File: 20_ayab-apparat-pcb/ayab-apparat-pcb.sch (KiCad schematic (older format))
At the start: 8 parts, among them P10 CONN_2, U1 NCP1117ST50T3G

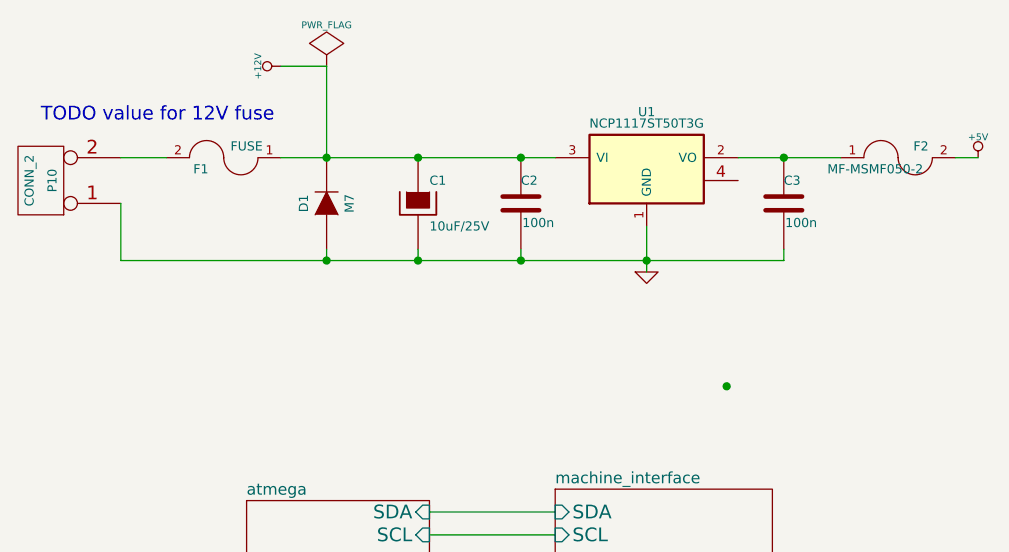
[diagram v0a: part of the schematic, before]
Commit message: BOM nearly done TODO add relais for autoswitch when USB 5V is connected to schematic
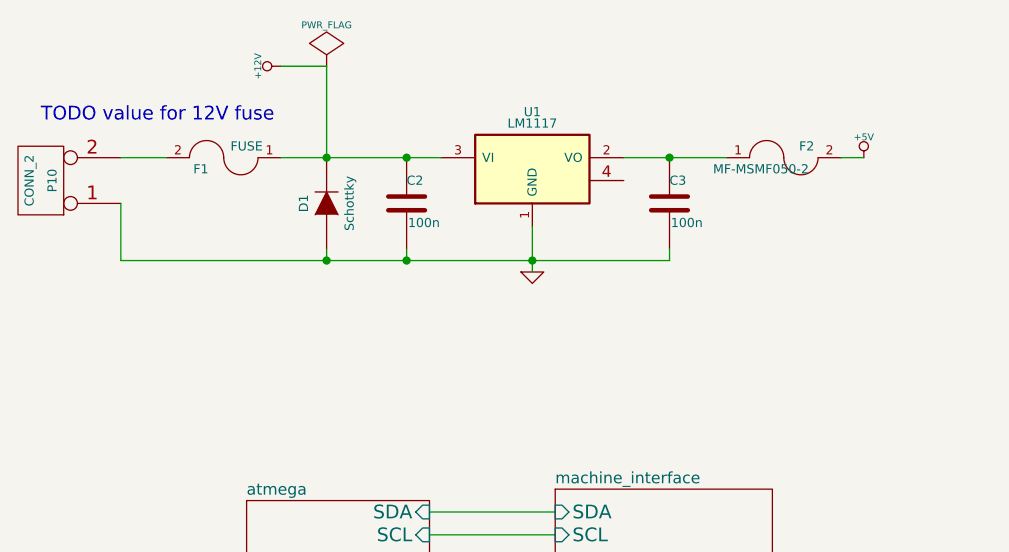
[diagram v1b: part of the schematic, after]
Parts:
- removed C1: 10uF/25V, symbol CAPAPOL
- D1: value M7 -> Schottky
- U1: value NCP1117ST50T3G -> LM1117
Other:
- moved on the sheet: C2, C3, F2, U1
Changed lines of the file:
@@
 $EndSheet
-$Comp
-L CAPAPOL C1
-U 1 1 52EAB7DE
-P 5400 2500
-F 0 "C1" H 5450 2600 40  0000 L CNN
-F 1 "10uF/25V" H 5450 2400 40  0000 L CNN
-F 2 "" H 5500 2350 30  0000 C CNN
-F 3 "" H 5400 2500 300 0000 C CNN
-	1    5400 2500
-	1    0    0    -1
-$EndComp
 $Comp
 L DIODE D1
@@
 P 5000 2500
 F 0 "D1" H 5000 2600 40  0000 C CNN
-F 1 "M7" H 5000 2400 40  0000 C CNN
+F 1 "Schottky" H 5000 2400 40  0000 C CNN
 F 2 "" H 5000 2500 60  0000 C CNN
 F 3 "" H 5000 2500 60  0000 C CNN
@@
 $EndComp
 $Comp
-L GND #PWR02
+L GND #PWR01
 U 1 1 52EABC97
-P 6400 2800
-F 0 "#PWR02" H 6400 2800 30  0001 C CNN
-F 1 "GND" H 6400 2730 30  0001 C CNN
-F 2 "" H 6400 2800 60  0000 C CNN
-F 3 "" H 6400 2800 60  0000 C CNN
-	1    6400 2800
+P 5900 2800
+F 0 "#PWR01" H 5900 2800 30  0001 C CNN
+F 1 "GND" H 5900 2730 30  0001 C CNN
+F 2 "" H 5900 2800 60  0000 C CNN
+F 3 "" H 5900 2800 60  0000 C CNN
+	1    5900 2800
 	1    0    0    -1
 $EndComp
@@
 L C C3
 U 1 1 52EAC19E
-P 7000 2500
-F 0 "C3" H 7000 2600 40  0000 L CNN
-F 1 "100n" H 7006 2415 40  0000 L CNN
-F 2 "" H 7038 2350 30  0000 C CNN
-F 3 "" H 7000 2500 60  0000 C CNN
-	1    7000 2500
+P 6500 2500
+F 0 "C3" H 6500 2600 40  0000 L CNN
+F 1 "100n" H 6506 2415 40  0000 L CNN
+F 2 "" H 6538 2350 30  0000 C CNN
+F 3 "" H 6500 2500 60  0000 C CNN
+	1    6500 2500
 	1    0    0    -1
 $EndComp
 $Comp
-L +5V #PWR03
+L +5V #PWR02
 U 1 1 52EAC279
-P 7850 2300
-F 0 "#PWR03" H 7850 2390 20  0001 C CNN
-F 1 "+5V" H 7850 2390 30  0000 C CNN
-F 2 "" H 7850 2300 60  0000 C CNN
-F 3 "" H 7850 2300 60  0000 C CNN
-	1    7850 2300
+P 7350 2300
+F 0 "#PWR02" H 7350 2390 20  0001 C CNN
+F 1 "+5V" H 7350 2390 30  0000 C CNN
+F 2 "" H 7350 2300 60  0000 C CNN
+F 3 "" H 7350 2300 60  0000 C CNN
+	1    7350 2300
 	1    0    0    -1
 $EndComp
 $Comp
-L +12V #PWR04
+L +12V #PWR03
 U 1 1 52EAEFAF
 P 4800 1900
-F 0 "#PWR04" H 4800 1850 20  0001 C CNN
+F 0 "#PWR03" H 4800 1850 20  0001 C CNN
 F 1 "+12V" H 4800 2000 30  0000 C CNN
 F 2 "" H 4800 1900 60  0000 C CNN
@@
 L FUSE F2
 U 1 1 52EAEFC3
-P 7500 2300
-F 0 "F2" H 7600 2350 40  0000 C CNN
-F 1 "MF-MSMF050-2" H 7400 2250 40  0000 C CNN
-F 2 "" H 7500 2300 60  0000 C CNN
-F 3 "" H 7500 2300 60  0000 C CNN
-	1    7500 2300
+P 7000 2300
+F 0 "F2" H 7100 2350 40  0000 C CNN
+F 1 "MF-MSMF050-2" H 6900 2250 40  0000 C CNN
+F 2 "" H 7000 2300 60  0000 C CNN
+F 3 "" H 7000 2300 60  0000 C CNN
+	1    7000 2300
 	1    0    0    -1
 $EndComp
@@
 TODO value for 12V fuse
 $Comp
-L PWR_FLAG #FLG05
+L PWR_FLAG #FLG04
 U 1 1 52EECA32
 P 5000 1900
-F 0 "#FLG05" H 5000 1995 30  0001 C CNN
+F 0 "#FLG04" H 5000 1995 30  0001 C CNN
 F 1 "PWR_FLAG" H 5000 2080 30  0000 C CNN
 F 2 "" H 5000 1900 60  0000 C CNN
@@
 L C C2
 U 1 1 52F1A256
-P 5850 2500
-F 0 "C2" H 5850 2600 40  0000 L CNN
-F 1 "100n" H 5856 2415 40  0000 L CNN
-F 2 "" H 5888 2350 30  0000 C CNN
-F 3 "" H 5850 2500 60  0000 C CNN
-	1    5850 2500
+P 5350 2500
+F 0 "C2" H 5350 2600 40  0000 L CNN
+F 1 "100n" H 5356 2415 40  0000 L CNN
+F 2 "" H 5388 2350 30  0000 C CNN
+F 3 "" H 5350 2500 60  0000 C CNN
+	1    5350 2500
 	1    0    0    -1
 $EndComp
@@
 L NCP1117ST50T3G U1
 U 1 1 52F1A2B7
-P 6400 2350
-F 0 "U1" H 6400 2600 40  0000 C CNN
-F 1 "NCP1117ST50T3G" H 6400 2550 40  0000 C CNN
-F 2 "" H 6400 2350 60  0000 C CNN
-F 3 "" H 6400 2350 60  0000 C CNN
-	1    6400 2350
+P 5900 2350
+F 0 "U1" H 5900 2600 40  0000 C CNN
+F 1 "LM1117" H 5900 2550 40  0000 C CNN
+F 2 "" H 5900 2350 60  0000 C CNN
+F 3 "" H 5900 2350 60  0000 C CNN
+	1    5900 2350
 	1    0    0    -1
 $EndComp
@@
 	5450 4700 6000 4700
 Wire Wire Line
-	4800 2300 6000 2300
+	4800 2300 5500 2300
 Wire Wire Line
-	6800 2300 7250 2300
+	6300 2300 6750 2300
 Wire Wire Line
-	4100 2750 7000 2750
-Connection ~ 7000 2300
+	4100 2750 6500 2750
+Connection ~ 6500 2300
 Wire Wire Line
-	7000 2750 7000 2700
+	6500 2750 6500 2700
 Wire Wire Line
-	7750 2300 7850 2300
+	7250 2300 7350 2300
 Wire Wire Line
 	5000 1900 5000 2300
@@
 Wire Wire Line
 	5000 2700 5000 2750
-Connection ~ 5400 2300
 Wire Wire Line
-	5400 2700 5400 2750
-Connection ~ 5400 2750
+	5350 2700 5350 2750
+Connection ~ 5350 2750
 Wire Wire Line
-	5850 2700 5850 2750
-Connection ~ 5850 2750
-Wire Wire Line
-	6400 2600 6400 2800
-Connection ~ 6400 2750
-Connection ~ 5850 2300
-Connection ~ 6750 3300
+	5900 2600 5900 2800
+Connection ~ 5900 2750
+Connection ~ 5350 2300
 Wire Wire Line
 	4100 2300 4300 2300

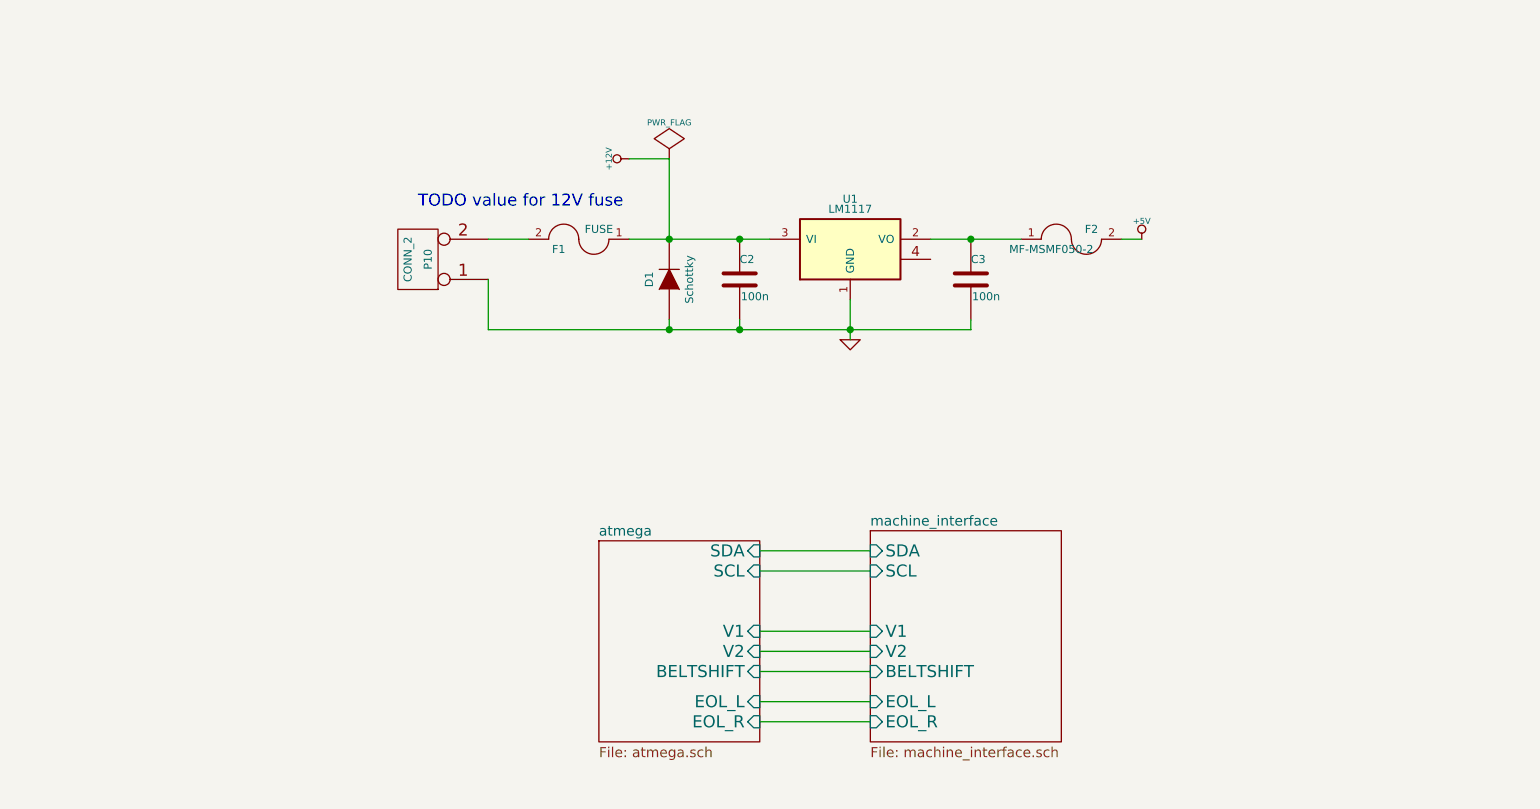
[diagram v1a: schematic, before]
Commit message: Added automatic switching between ATmega and original machine control when VUSB is attached
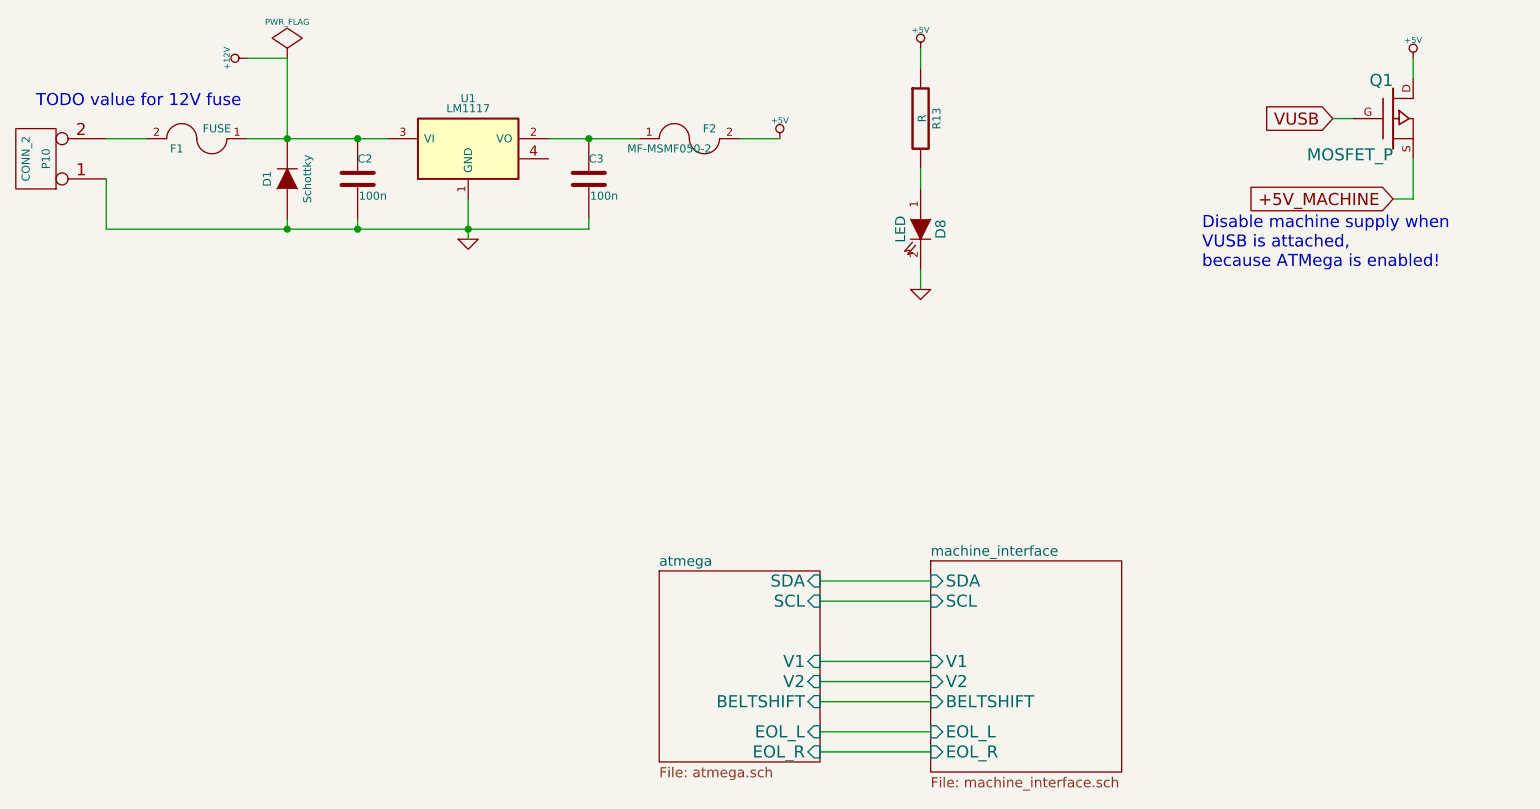
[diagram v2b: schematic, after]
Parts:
- added D8: LED, symbol LED
- added Q1: MOSFET_P, symbol MOSFET_P
- added R13: R, symbol R
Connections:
- net +5V: now also Q1.D, R13.1
- net GND: now also D8.2 (K)
- new net: D8.1 (A), R13.2
- new net +5V_MACHINE: Q1.S
- new net VUSB: Q1.G
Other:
- note added: "Disable machine supply when\nVUSB is attached,\nbecause ATMega is enabled!"
- moved on the sheet: C2, C3, D1, F1, F2, P10, U1

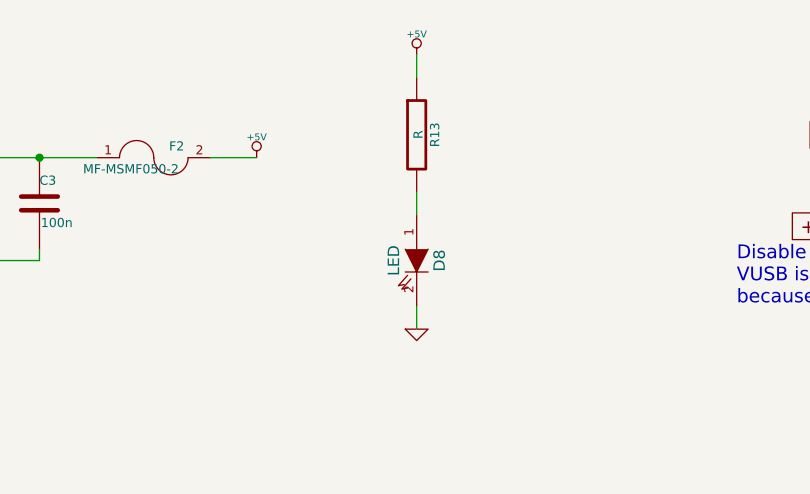
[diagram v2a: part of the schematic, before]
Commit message: Changed power supply of ATMega to VUSB finished BOM CSV -> ready to layout
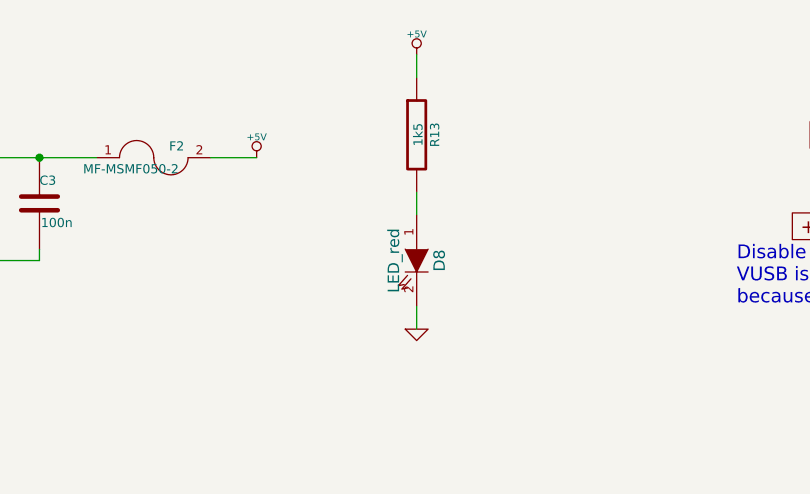
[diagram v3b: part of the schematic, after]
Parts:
- D8: value LED -> LED_red
- R13: value R -> 1k5
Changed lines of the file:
@@
 P 6250 1700
 F 0 "R13" V 6330 1700 40  0000 C CNN
-F 1 "R" V 6257 1701 40  0000 C CNN
+F 1 "1k5" V 6257 1701 40  0000 C CNN
 F 2 "" V 6180 1700 30  0000 C CNN
 F 3 "" H 6250 1700 30  0000 C CNN
@@
 P 6250 2250
 F 0 "D8" H 6250 2350 50  0000 C CNN
-F 1 "LED" H 6250 2150 50  0000 C CNN
+F 1 "LED_red" H 6250 2150 50  0000 C CNN
 F 2 "" H 6250 2250 60  0000 C CNN
 F 3 "" H 6250 2250 60  0000 C CNN

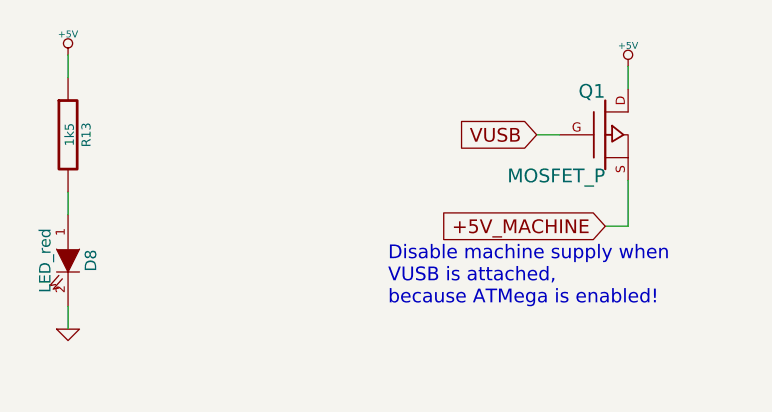
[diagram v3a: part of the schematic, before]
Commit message: Added resistor for MOSFET gate
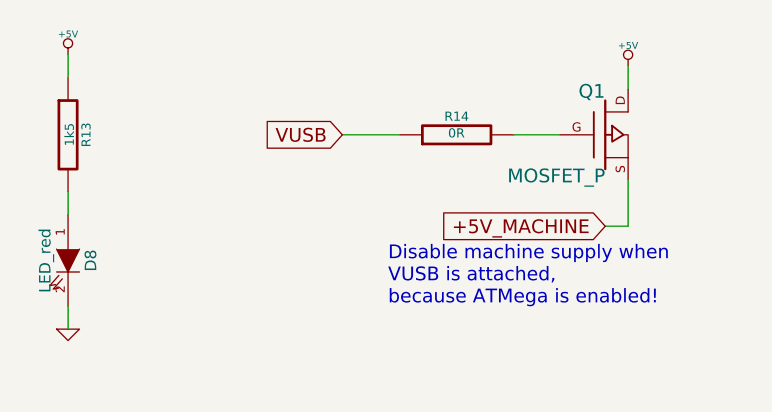
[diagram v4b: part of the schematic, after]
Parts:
- added R14: 0R, symbol R
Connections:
- net VUSB: now also R14.1; no longer Q1.G
- new net: Q1.G, R14.2
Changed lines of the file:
@@
 $EndComp
 $Comp
-L GND #PWR01
+L GND #PWR2
 U 1 1 52EABC97
 P 4000 2300
-F 0 "#PWR01" H 4000 2300 30  0001 C CNN
+F 0 "#PWR2" H 4000 2300 30  0001 C CNN
 F 1 "GND" H 4000 2230 30  0001 C CNN
 F 2 "" H 4000 2300 60  0000 C CNN
@@
 $EndComp
 $Comp
-L +5V #PWR02
+L +5V #PWR3
 U 1 1 52EAC279
 P 5550 1800
-F 0 "#PWR02" H 5550 1890 20  0001 C CNN
+F 0 "#PWR3" H 5550 1890 20  0001 C CNN
 F 1 "+5V" H 5550 1890 30  0000 C CNN
 F 2 "" H 5550 1800 60  0000 C CNN
@@
 $EndComp
 $Comp
-L +12V #PWR03
+L +12V #PWR1
 U 1 1 52EAEFAF
 P 2900 1400
-F 0 "#PWR03" H 2900 1350 20  0001 C CNN
+F 0 "#PWR1" H 2900 1350 20  0001 C CNN
 F 1 "+12V" H 2900 1500 30  0000 C CNN
 F 2 "" H 2900 1400 60  0000 C CNN
@@
 TODO value for 12V fuse
 $Comp
-L PWR_FLAG #FLG04
+L PWR_FLAG #FLG1
 U 1 1 52EECA32
 P 3100 1400
-F 0 "#FLG04" H 3100 1495 30  0001 C CNN
+F 0 "#FLG1" H 3100 1495 30  0001 C CNN
 F 1 "PWR_FLAG" H 3100 1580 30  0000 C CNN
 F 2 "" H 3100 1400 60  0000 C CNN
@@
 $EndComp
 $Comp
-L +5V #PWR05
+L +5V #PWR6
 U 1 1 5302828E
 P 8700 1400
-F 0 "#PWR05" H 8700 1490 20  0001 C CNN
+F 0 "#PWR6" H 8700 1490 20  0001 C CNN
 F 1 "+5V" H 8700 1490 30  0000 C CNN
 F 2 "" H 8700 1400 60  0000 C CNN
@@
 Wire Wire Line
 	8700 2100 8700 1900
-Text GLabel 8300 1700 0    60   Input ~ 0
+Text GLabel 7450 1700 0    60   Input ~ 0
 VUSB
-Wire Wire Line
-	8300 1700 8400 1700
 Text Notes 7650 2450 0    60   ~ 0
 Disable machine supply when\nVUSB is attached,\nbecause ATMega is enabled!
@@
 $EndComp
 $Comp
-L +5V #PWR06
+L +5V #PWR4
 U 1 1 5302A625
 P 6250 1350
-F 0 "#PWR06" H 6250 1440 20  0001 C CNN
+F 0 "#PWR4" H 6250 1440 20  0001 C CNN
 F 1 "+5V" H 6250 1440 30  0000 C CNN
 F 2 "" H 6250 1350 60  0000 C CNN
@@
 $EndComp
 $Comp
-L GND #PWR07
+L GND #PWR5
 U 1 1 5302A639
 P 6250 2550
-F 0 "#PWR07" H 6250 2550 30  0001 C CNN
+F 0 "#PWR5" H 6250 2550 30  0001 C CNN
 F 1 "GND" H 6250 2480 30  0001 C CNN
 F 2 "" H 6250 2550 60  0000 C CNN
@@
 Wire Wire Line
 	6250 1450 6250 1350
+$Comp
+L R R14
+U 1 1 5305130C
+P 7950 1700
+F 0 "R14" V 8030 1700 40  0000 C CNN
+F 1 "0R" V 7957 1701 40  0000 C CNN
+F 2 "" V 7880 1700 30  0000 C CNN
+F 3 "" H 7950 1700 30  0000 C CNN
+	1    7950 1700
+	0    -1   -1   0
+$EndComp
+Wire Wire Line
+	7450 1700 7700 1700
+Wire Wire Line
+	8200 1700 8400 1700
 $EndSCHEMATC

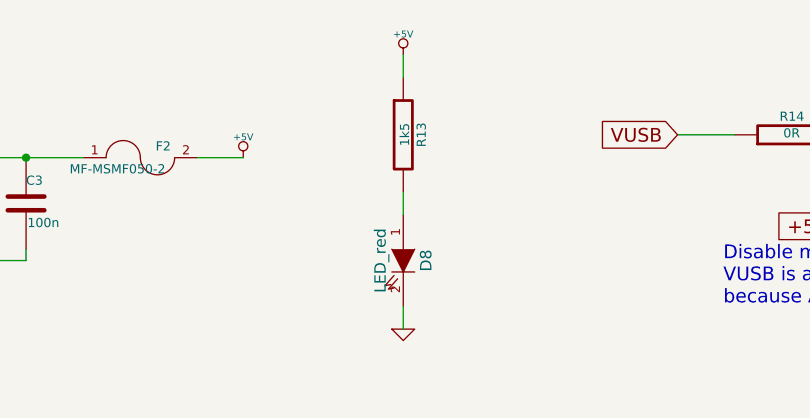
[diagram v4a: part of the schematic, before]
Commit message: fixed LED resistor value
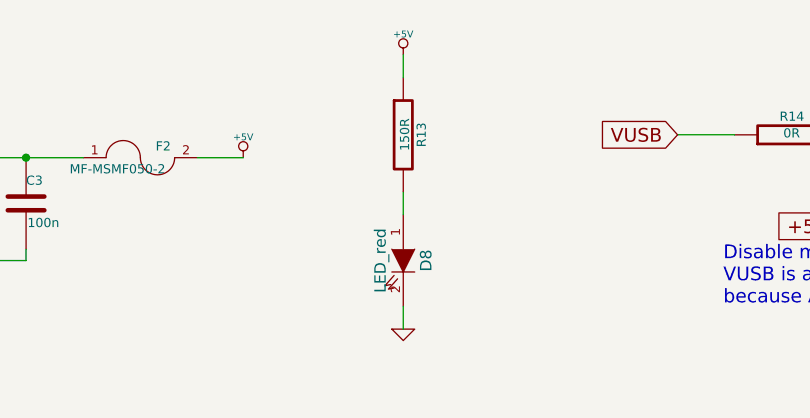
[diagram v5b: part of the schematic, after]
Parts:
- R13: value 1k5 -> 150R
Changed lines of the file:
@@
 $EndComp
 $Comp
-L GND #PWR2
+L GND #PWR01
 U 1 1 52EABC97
 P 4000 2300
-F 0 "#PWR2" H 4000 2300 30  0001 C CNN
+F 0 "#PWR01" H 4000 2300 30  0001 C CNN
 F 1 "GND" H 4000 2230 30  0001 C CNN
 F 2 "" H 4000 2300 60  0000 C CNN
@@
 $EndComp
 $Comp
-L +5V #PWR3
+L +5V #PWR02
 U 1 1 52EAC279
 P 5550 1800
-F 0 "#PWR3" H 5550 1890 20  0001 C CNN
+F 0 "#PWR02" H 5550 1890 20  0001 C CNN
 F 1 "+5V" H 5550 1890 30  0000 C CNN
 F 2 "" H 5550 1800 60  0000 C CNN
@@
 $EndComp
 $Comp
-L +12V #PWR1
+L +12V #PWR03
 U 1 1 52EAEFAF
 P 2900 1400
-F 0 "#PWR1" H 2900 1350 20  0001 C CNN
+F 0 "#PWR03" H 2900 1350 20  0001 C CNN
 F 1 "+12V" H 2900 1500 30  0000 C CNN
 F 2 "" H 2900 1400 60  0000 C CNN
@@
 TODO value for 12V fuse
 $Comp
-L PWR_FLAG #FLG1
+L PWR_FLAG #FLG04
 U 1 1 52EECA32
 P 3100 1400
-F 0 "#FLG1" H 3100 1495 30  0001 C CNN
+F 0 "#FLG04" H 3100 1495 30  0001 C CNN
 F 1 "PWR_FLAG" H 3100 1580 30  0000 C CNN
 F 2 "" H 3100 1400 60  0000 C CNN
@@
 $EndComp
 $Comp
-L +5V #PWR6
+L +5V #PWR05
 U 1 1 5302828E
 P 8700 1400
-F 0 "#PWR6" H 8700 1490 20  0001 C CNN
+F 0 "#PWR05" H 8700 1490 20  0001 C CNN
 F 1 "+5V" H 8700 1490 30  0000 C CNN
 F 2 "" H 8700 1400 60  0000 C CNN
@@
 P 6250 1700
 F 0 "R13" V 6330 1700 40  0000 C CNN
-F 1 "1k5" V 6257 1701 40  0000 C CNN
+F 1 "150R" V 6257 1701 40  0000 C CNN
 F 2 "" V 6180 1700 30  0000 C CNN
 F 3 "" H 6250 1700 30  0000 C CNN
@@
 $EndComp
 $Comp
-L +5V #PWR4
+L +5V #PWR06
 U 1 1 5302A625
 P 6250 1350
-F 0 "#PWR4" H 6250 1440 20  0001 C CNN
+F 0 "#PWR06" H 6250 1440 20  0001 C CNN
 F 1 "+5V" H 6250 1440 30  0000 C CNN
 F 2 "" H 6250 1350 60  0000 C CNN
@@
 $EndComp
 $Comp
-L GND #PWR5
+L GND #PWR07
 U 1 1 5302A639
 P 6250 2550
-F 0 "#PWR5" H 6250 2550 30  0001 C CNN
+F 0 "#PWR07" H 6250 2550 30  0001 C CNN
 F 1 "GND" H 6250 2480 30  0001 C CNN
 F 2 "" H 6250 2550 60  0000 C CNN

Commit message: ayab-apparat v2 ready for review
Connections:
- net at C3.1, F2.1, U1.2 (VO): now also U1.4
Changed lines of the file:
@@
 Wire Wire Line
 	8200 1700 8400 1700
+Wire Wire Line
+	4400 1900 4500 1900
+Wire Wire Line
+	4500 1900 4500 1800
+Connection ~ 4500 1800
 $EndSCHEMATC
